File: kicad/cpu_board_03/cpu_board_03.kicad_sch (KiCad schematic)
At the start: 63 parts, among them J1 DIN41612_02x32_AC, J10 PLD_aux, J11 Conn_01x09, J6 Conn_01x02_Socket, J9 Ram1 Enable, SW1 SW_Reset, SW2 SW_PWR, U1 W65C02SxP, U10 74HC245, U11 74HC245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

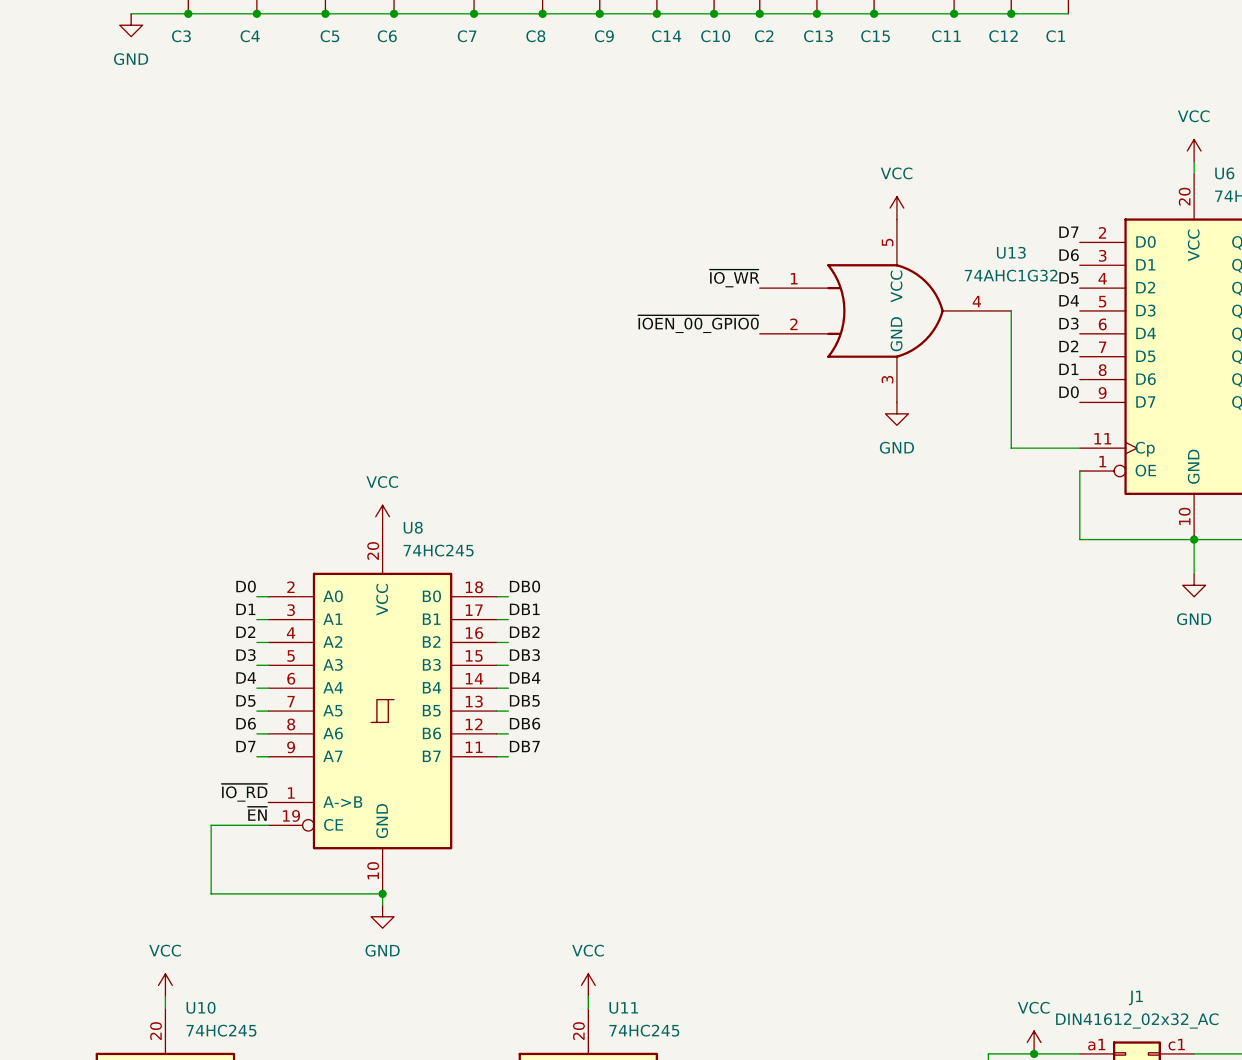
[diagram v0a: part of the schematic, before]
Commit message: add bus tranceiver OE signal
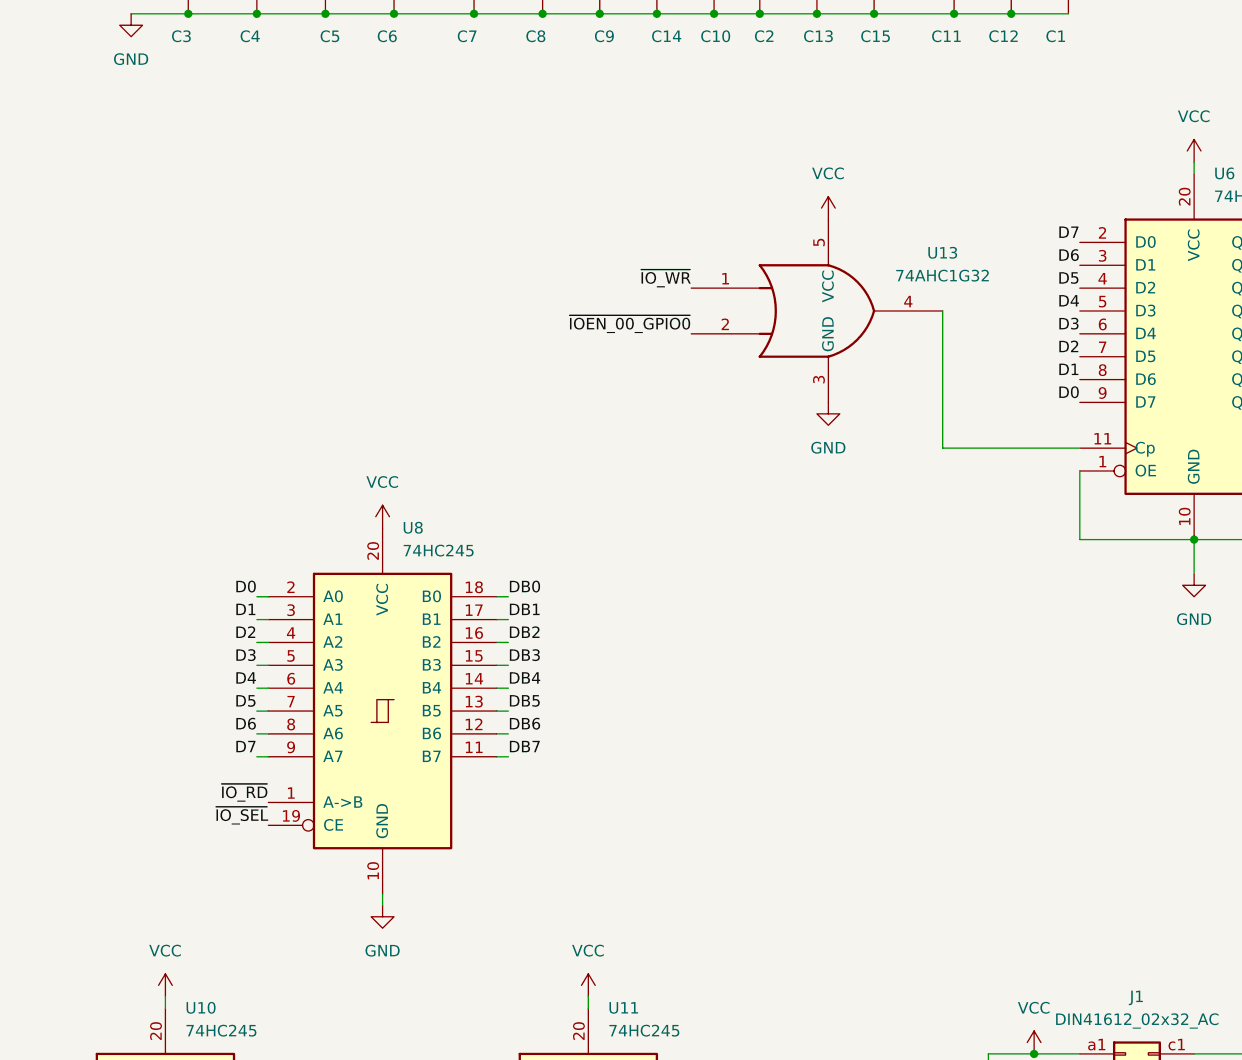
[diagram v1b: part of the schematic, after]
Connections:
- net GND: no longer U8.19 (CE)
- net ~{IO_SEL}: now also U8.19 (CE)
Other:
- moved on the sheet: U13
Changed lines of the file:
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@@
 	)
 	(junction
-		(at 271.78 147.32)
-		(diameter 0)
-		(color 0 0 0 0)
-	)
-	(junction
 		(at 261.62 241.3)
 		(diameter 0)
@@
 	(wire
 		(pts
-			(xy 252.73 147.32) (xy 252.73 139.7)
-		)
-		(stroke
-			(width 0)
-			(type default)
-		)
-	)
-	(wire
-		(pts
 			(xy 313.69 41.91) (xy 320.04 41.91)
 		)
@@
 	(wire
 		(pts
-			(xy 252.73 139.7) (xy 259.08 139.7)
-		)
-		(stroke
-			(width 0)
-			(type default)
-		)
-	)
-	(wire
-		(pts
 			(xy 271.78 228.6) (xy 278.13 228.6)
 		)
@@
 	(wire
 		(pts
-			(xy 341.63 82.55) (xy 341.63 97.79)
+			(xy 334.01 82.55) (xy 334.01 97.79)
 		)
 		(stroke
@@
 	(wire
 		(pts
-			(xy 271.78 147.32) (xy 252.73 147.32)
-		)
-		(stroke
-			(width 0)
-			(type default)
-		)
-	)
-	(wire
-		(pts
-			(xy 341.63 97.79) (xy 349.25 97.79)
+			(xy 334.01 97.79) (xy 349.25 97.79)
 		)
 		(stroke
@@
 		)
 	)
-	(label "~{EN}"
-		(at 259.08 139.7 180)
-		(effects
-			(font
-				(size 1.27 1.27)
-			)
-			(justify right bottom)
-		)
-	)
 	(label "D2"
 		(at 162.56 140.97 0)
@@
 	)
 	(label "~{IO_WR}"
-		(at 313.69 80.01 180)
+		(at 306.07 80.01 180)
 		(effects
 			(font
@@
 		)
 	)
+	(label "~{IO_SEL}"
+		(at 259.08 139.7 180)
+		(effects
+			(font
+				(size 1.27 1.27)
+			)
+			(justify right bottom)
+		)
+	)
 	(label "A11"
 		(at 134.62 163.83 180)
@@
 	)
 	(label "~{IOEN_00_GPIO0}"
-		(at 313.69 85.09 180)
+		(at 306.07 85.09 180)
 		(effects
 			(font
@@
 	(symbol
 		(lib_id "74xGxx:74AHC1G32")
-		(at 328.93 82.55 0)
+		(at 321.31 82.55 0)
 		(unit 1)
 		(exclude_from_sim no)
@@
 		(fields_autoplaced yes)
 		(property "Reference" "U13"
-			(at 341.63 76.1298 0)
+			(at 334.01 76.1298 0)
 			(effects
 				(font
@@
 		)
 		(property "Value" "74AHC1G32"
-			(at 341.63 78.6698 0)
+			(at 334.01 78.6698 0)
 			(effects
 				(font
@@
 		)
 		(property "Footprint" "Package_TO_SOT_SMD:SOT-23-5_HandSoldering"
-			(at 328.93 82.55 0)
+			(at 321.31 82.55 0)
 			(effects
 				(font
@@
 		)
 		(property "Datasheet" "http://www.ti.com/lit/sg/scyt129e/scyt129e.pdf"
-			(at 328.93 82.55 0)
+			(at 321.31 82.55 0)
 			(effects
 				(font
@@
 		)
 		(property "Description" "Single OR Gate, Low-Voltage CMOS"
-			(at 328.93 82.55 0)
+			(at 321.31 82.55 0)
 			(effects
 				(font
@@
 	(symbol
 		(lib_id "power:GND")
-		(at 328.93 92.71 0)
+		(at 321.31 92.71 0)
 		(unit 1)
 		(exclude_from_sim no)
@@
 		(fields_autoplaced yes)
 		(property "Reference" "#PWR042"
-			(at 328.93 99.06 0)
+			(at 321.31 99.06 0)
 			(effects
 				(font
@@
 		)
 		(property "Value" "GND"
-			(at 328.93 97.79 0)
+			(at 321.31 97.79 0)
 			(effects
 				(font
@@
 		)
 		(property "Footprint" ""
-			(at 328.93 92.71 0)
+			(at 321.31 92.71 0)
 			(effects
 				(font
@@
 		)
 		(property "Datasheet" ""
-			(at 328.93 92.71 0)
+			(at 321.31 92.71 0)
 			(effects
 				(font
@@
 		)
 		(property "Description" ""
-			(at 328.93 92.71 0)
+			(at 321.31 92.71 0)
 			(effects
 				(font
@@
 	(symbol
 		(lib_id "power:VCC")
-		(at 328.93 72.39 0)
+		(at 321.31 72.39 0)
 		(unit 1)
 		(exclude_from_sim no)
@@
 		(fields_autoplaced yes)
 		(property "Reference" "#PWR045"
-			(at 328.93 76.2 0)
+			(at 321.31 76.2 0)
 			(effects
 				(font
@@
 		)
 		(property "Value" "VCC"
-			(at 328.93 67.31 0)
+			(at 321.31 67.31 0)
 			(effects
 				(font
@@
 		)
 		(property "Footprint" ""
-			(at 328.93 72.39 0)
+			(at 321.31 72.39 0)
 			(effects
 				(font
@@
 		)
 		(property "Datasheet" ""
-			(at 328.93 72.39 0)
+			(at 321.31 72.39 0)
 			(effects
 				(font
@@
 		)
 		(property "Description" ""
-			(at 328.93 72.39 0)
+			(at 321.31 72.39 0)
 			(effects
 				(font

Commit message: route latest changes
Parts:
- removed J10: PLD_aux, Connector_PinHeader_2.54mm:PinHeader_1x03_P2.54mm_Vertical, symbol Connector:Conn_01x03_Socket
- removed R8: 10K, Resistor_SMD:R_0805_2012Metric_Pad1.20x1.40mm_HandSolder, symbol Device:R
- removed U11: 74HC245, Package_SO:SO-20_12.8x7.5mm_P1.27mm, symbol 74xx:74HC245
- removed U12: 74LS138, Package_SO:SO-16_3.9x9.9mm_P1.27mm, symbol 74xx:74LS138
- added JP1, JP2: SolderJumper_3_Open, Jumper:SolderJumper-3_P1.3mm_Bridged12_RoundedPad1.0x1.5mm_NumberLabels, symbol Jumper:SolderJumper_3_Bridged12
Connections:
- net AB10 is gone; now on net AB2: J1.a13 (Pin_a13)
- net AB11 is gone; now on net AB3: J1.c13 (Pin_c13)
- net AB12 is gone; now on net AB4: J1.a12 (Pin_a12)
- net AB13 is gone; now on net ~{IO_RD}: J1.c12 (Pin_c12)
- net AB14 is gone; now on net ~{IO_WR}: J1.a11 (Pin_a11)
- net AB8 is gone; now on net AB0: J1.a14 (Pin_a14)
- net AB9 is gone; now on net AB1: J1.c14 (Pin_c14)
- net ~{IOEN_12} is gone; now on net RDY: J1.a22 (Pin_a22)
- net ~{IOEN_13} is gone; now on net ~{IRQ}: J1.c22 (Pin_c22)
- net ~{IOEN_14} is gone; now on net ~{NMI}: J1.a21 (Pin_a21)
- net ~{IOEN_15} is gone; now on net SYNC: J1.c21 (Pin_c21)
- net A4: no longer U5.1 (A0)
- net A5: now also U5.1 (A0); no longer U10.13 (B5), U5.2 (A1)
- net A6: now also U5.2 (A1); no longer U10.12 (B6), U5.3 (A2)
- net A7: now also U5.3 (A2); no longer U10.11 (B7), U5.5 (E2)
- net AB0: no longer J1.a18 (Pin_a18)
- net AB1: no longer J1.c18 (Pin_c18)
- net AB2: no longer J1.a17 (Pin_a17)
- net AB3: no longer J1.c17 (Pin_c17)
- net AB4: no longer J1.a16 (Pin_a16)
- net CLOCK: now also J1.a7 (Pin_a7)
- net GND: now also J1.c15 (Pin_c15), U5.5 (E2); no longer J1.c19 (Pin_c19)
- net PLD_I1: now also J1.c9 (Pin_c9)
- net RDY: no longer J1.c29 (Pin_c29)
- net SYS_CLK: now also U4.23 (O0); no longer J1.a7 (Pin_a7), U4.15 (O8)
- net VCC: now also J1.a15 (Pin_a15); no longer J1.a19 (Pin_a19)
- net ~{IOEN_00_GPIO0}: now also J1.a19 (Pin_a19), U13.1; no longer J1.a28 (Pin_a28), U13.2
- net ~{IOEN_01}: now also J1.c19 (Pin_c19); no longer J1.c28 (Pin_c28)
- net ~{IOEN_02_UART}: now also J1.a18 (Pin_a18); no longer J1.a27 (Pin_a27)
- net ~{IOEN_03}: now also J1.c18 (Pin_c18); no longer J1.c27 (Pin_c27)
- net ~{IOEN_04}: now also J1.a17 (Pin_a17); no longer J1.a26 (Pin_a26)
- net ~{IOEN_05}: now also J1.c17 (Pin_c17); no longer J1.c26 (Pin_c26)
- net ~{IOEN_06}: now also J1.a16 (Pin_a16); no longer J1.a25 (Pin_a25)
- net ~{IOEN_07}: now also J1.c16 (Pin_c16); no longer J1.c25 (Pin_c25)
- net ~{IO_RD}: now also U10.7 (A5); no longer J1.c8 (Pin_c8), U4.16 (O7)
- net ~{IO_SEL}: now also U10.11 (B7); no longer J1.a8 (Pin_a8)
- net ~{IO_WR}: now also U10.8 (A6), U13.2; no longer J1.c7 (Pin_c7), U13.1, U4.14 (O9)
- net ~{IRQ}: no longer J1.a29 (Pin_a29)
- net ~{NMI}: no longer J1.c30 (Pin_c30)
- net ~{OE}: now also JP1.1 (A)
- net ~{QWE}: now also JP2.1 (A)
- net SYNC: now reaches U1.7 (SYNC)
- net AB15 renamed ~{IO_SEL_BUS}
- net ~{IO_SEL_BUS}: now also U10.9 (A7)
- removed net AB5: J1.c16 (Pin_c16), U10.7 (A5)
- removed net AB6: J1.a15 (Pin_a15), U10.8 (A6)
- removed net AB7: J1.c15 (Pin_c15), U10.9 (A7)
- net BE: no longer names the net of U1.36 (BE)
- net BE: no longer J1.a30 (Pin_a30)
- removed net PLD_O0: J1.c9 (Pin_c9), U4.23 (O0)
- net ~{IOEN_08}: no longer names the net of J1.a24 (Pin_a24)
- net ~{IOEN_09}: no longer names the net of J1.c24 (Pin_c24)
- net ~{IOEN_10}: no longer names the net of J1.a23 (Pin_a23)
- net ~{IOEN_11}: no longer names the net of J1.c23 (Pin_c23)
- new net: JP2.2 (C), U10.12 (B6)
- new net: JP1.2 (C), U10.13 (B5)
- new net PLD_O7: J1.c8 (Pin_c8), JP1.3 (B), U4.16 (O7)
- new net PLD_O8: J1.a8 (Pin_a8), JP2.3 (B), U4.15 (O8)
- new net PLD_O9: J1.c7 (Pin_c7), U4.14 (O9)
- no-connect marks 12 -> 14

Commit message: finished basic routing
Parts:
- added J2: Clock, Connector_PinSocket_2.54mm:PinSocket_1x02_P2.54mm_Vertical, symbol Connector:Conn_01x02_Socket
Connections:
- net CLOCK: now also J2.2 (Pin_2); no longer J1.a7 (Pin_a7)
- net GND: now also J2.1 (Pin_1)
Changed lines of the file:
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@@
 	(generator_version "9.0")
 	(paper "A3")
-	(text_box "v2.1 update: connect ~{E2} to A7 to select onboard IO (IO0) only for io addresses 0x00 - 0x7f\n0x80-0xff can be used on external io board"
+	(text_box "v3 update: select IO port from highest 3 bits only."
 		(exclude_from_sim no)
 		(at 83.82 265.43 0)
@@
 		(stroke
 			(width 0)
-			(type default)
+			(type solid)
 		)
 		(fill
@@
 		)
 	)
+	(label "CLOCK"
+		(at 59.69 82.55 180)
+		(effects
+			(font
+				(size 1.27 1.27)
+			)
+			(justify right bottom)
+		)
+	)
 	(label "DB7"
 		(at 361.95 167.64 0)
@@
 		)
 	)
-	(label "CLOCK"
-		(at 349.25 180.34 180)
-		(effects
-			(font
-				(size 1.27 1.27)
-			)
-			(justify right bottom)
-		)
-	)
 	(label "A3"
 		(at 134.62 143.51 180)
@@
 	)
 	(symbol
+		(lib_id "power:GND")
+		(at 59.69 85.09 0)
+		(unit 1)
+		(exclude_from_sim no)
+		(in_bom yes)
+		(on_board yes)
+		(dnp no)
+		(fields_autoplaced yes)
+		(property "Reference" "#PWR027"
+			(at 59.69 91.44 0)
+			(effects
+				(font
+					(size 1.27 1.27)
+				)
+				(hide yes)
+			)
+		)
+		(property "Value" "GND"
+			(at 59.69 90.17 0)
+			(effects
+				(font
+					(size 1.27 1.27)
+				)
+			)
+		)
+		(property "Footprint" ""
+			(at 59.69 85.09 0)
+			(effects
+				(font
+					(size 1.27 1.27)
+				)
+				(hide yes)
+			)
+		)
+		(property "Datasheet" ""
+			(at 59.69 85.09 0)
+			(effects
+				(font
+					(size 1.27 1.27)
+				)
+				(hide yes)
+			)
+		)
+		(property "Description" ""
+			(at 59.69 85.09 0)
+			(effects
+				(font
+					(size 1.27 1.27)
+				)
+			)
+		)
+		(pin "1"
+		)
+		(instances
+			(project "cpu_board_03"
+				(path "/a9a73dc6-7f92-4458-9da8-49621d12e480"
+					(reference "#PWR027")
+					(unit 1)
+				)
+			)
+		)
+	)
+	(symbol
 		(lib_id "Device:C")
 		(at 265.43 45.72 0)
@@
 					(unit 1)
 				)
+			)
+		)
+	)
+	(symbol
+		(lib_id "Connector:Conn_01x02_Socket")
+		(at 64.77 85.09 0)
+		(mirror x)
+		(unit 1)
+		(exclude_from_sim no)
+		(in_bom yes)
+		(on_board yes)
+		(dnp no)
+		(property "Reference" "J2"
+			(at 67.818 86.868 0)
+			(effects
+				(font
+					(size 1.27 1.27)
+				)
+			)
+		)
+		(property "Value" "Clock"
+			(at 62.23 85.09 90)
+			(effects
+				(font
+					(size 1.27 1.27)
+				)
+			)
+		)
+		(property "Footprint" "Connector_PinSocket_2.54mm:PinSocket_1x02_P2.54mm_Vertical"
+			(at 64.77 85.09 0)
+			(effects
+				(font
+					(size 1.27 1.27)
+				)
+				(hide yes)
+			)
+		)
+		(property "Datasheet" "~"
+			(at 64.77 85.09 0)
+			(effects
+				(font
+					(size 1.27 1.27)
+				)
+				(hide yes)
+			)
+		)
+		(property "Description" "Generic connector, single row, 01x02, script generated"
+			(at 64.77 85.09 0)
+			(effects
+				(font
+					(size 1.27 1.27)
+				)
+				(hide yes)
+			)
+		)
+		(pin "1"
+		)
+		(pin "2"
+		)
+		(instances
+			(project "cpu_board_03"
+				(path "/a9a73dc6-7f92-4458-9da8-49621d12e480"
+					(reference "J2")
+					(unit 1)
+				)

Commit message: finished drc errors
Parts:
- removed C15: 100nF, Capacitor_SMD:C_0805_2012Metric_Pad1.18x1.45mm_HandSolder, symbol Device:C
- added JP3: SolderJumper_3_Open, Jumper:SolderJumper-3_P1.3mm_Open_RoundedPad1.0x1.5mm, symbol Jumper:SolderJumper_3_Open
- JP1, JP2: footprint Jumper:SolderJumper-3_P1.3mm_Bridged12_RoundedPad1.0x1.5mm_NumberLabels -> Jumper:SolderJumper-3_P1.3mm_Open_RoundedPad1.0x1.5mm; symbol Jumper:SolderJumper_3_Bridged12 -> Jumper:SolderJumper_3_Open
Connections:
- net A4: now also JP3.3 (B)
- net GND: now also JP3.1 (A); no longer U5.5 (E2)
- new net: JP3.2 (C), U5.5 (E2)
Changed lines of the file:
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@@
 	(text_box "v3 update: select IO port from highest 3 bits only."
 		(exclude_from_sim no)
-		(at 83.82 265.43 0)
+		(at 68.58 276.86 0)
 		(size 24.13 17.78)
 		(margins 0.9525 0.9525 0.9525 0.9525)
@@
 	)
 	(junction
-		(at 326.39 49.53)
-		(diameter 0)
-		(color 0 0 0 0)
-	)
-	(junction
 		(at 361.95 107.95)
 		(diameter 0)
@@
 	)
 	(junction
-		(at 326.39 41.91)
-		(diameter 0)
-		(color 0 0 0 0)
-	)
-	(junction
 		(at 339.09 200.66)
 		(diameter 0)
@@
 	(wire
 		(pts
-			(xy 99.06 260.35) (xy 99.06 275.59)
+			(xy 95.25 254) (xy 95.25 255.27)
 		)
 		(stroke
@@
 	(wire
 		(pts
-			(xy 320.04 41.91) (xy 326.39 41.91)
+			(xy 339.09 187.96) (xy 339.09 200.66)
 		)
 		(stroke
@@
 	(wire
 		(pts
-			(xy 339.09 187.96) (xy 339.09 200.66)
+			(xy 128.27 25.4) (xy 135.89 25.4)
 		)
 		(stroke
@@
 	(wire
 		(pts
-			(xy 128.27 25.4) (xy 135.89 25.4)
+			(xy 92.71 254) (xy 95.25 254)
 		)
 		(stroke
@@
 	(wire
 		(pts
+			(xy 95.25 275.59) (xy 119.38 275.59)
+		)
+		(stroke
+			(width 0)
+			(type default)
+		)
+	)
+	(wire
+		(pts
 			(xy 25.4 266.7) (xy 35.56 266.7)
 		)
@@
 	(wire
 		(pts
-			(xy 99.06 275.59) (xy 119.38 275.59)
-		)
-		(stroke
-			(width 0)
-			(type default)
-		)
-	)
-	(wire
-		(pts
 			(xy 110.49 151.13) (xy 109.22 151.13)
 		)
@@
 	(wire
 		(pts
-			(xy 326.39 49.53) (xy 335.28 49.53)
+			(xy 320.04 49.53) (xy 335.28 49.53)
 		)
 		(stroke
@@
 	(wire
 		(pts
-			(xy 326.39 41.91) (xy 335.28 41.91)
+			(xy 320.04 41.91) (xy 335.28 41.91)
 		)
 		(stroke
@@
 	(wire
 		(pts
-			(xy 320.04 49.53) (xy 326.39 49.53)
-		)
-		(stroke
-			(width 0)
-			(type default)
-		)
-	)
-	(wire
-		(pts
 			(xy 273.05 242.57) (xy 278.13 242.57)
 		)
@@
 	(wire
 		(pts
+			(xy 95.25 275.59) (xy 95.25 265.43)
+		)
+		(stroke
+			(width 0)
+			(type default)
+		)
+	)
+	(wire
+		(pts
 			(xy 58.42 121.92) (xy 57.15 121.92)
 		)
@@
 		)
 	)
+	(label "A4"
+		(at 92.71 254 0)
+		(effects
+			(font
+				(size 1.27 1.27)
+			)
+			(justify left bottom)
+		)
+	)
 	(label "DB6"
 		(at 349.25 167.64 180)
@@
 	)
 	(symbol
-		(lib_id "Device:C")
-		(at 326.39 45.72 0)
-		(unit 1)
-		(exclude_from_sim no)
-		(in_bom yes)
-		(on_board yes)
-		(dnp no)
-		(property "Reference" "C15"
-			(at 328.295 52.07 0)
-			(effects
-				(font
-					(size 1.27 1.27)
-				)
-				(justify right)
-			)
-		)
-		(property "Value" "100nF"
-			(at 328.93 39.37 0)
-			(effects
-				(font
-					(size 1.27 1.27)
-				)
-				(justify right)
-			)
-		)
-		(property "Footprint" "Capacitor_SMD:C_0805_2012Metric_Pad1.18x1.45mm_HandSolder"
-			(at 327.3552 49.53 0)
-			(effects
-				(font
-					(size 1.27 1.27)
-				)
-				(hide yes)
-			)
-		)
-		(property "Datasheet" "~"
-			(at 326.39 45.72 0)
-			(effects
-				(font
-					(size 1.27 1.27)
-				)
-				(hide yes)
-			)
-		)
-		(property "Description" ""
-			(at 326.39 45.72 0)
-			(effects
-				(font
-					(size 1.27 1.27)
-				)
-			)
-		)
-		(pin "1"
-		)
-		(pin "2"
-		)
-		(instances
-			(project "cpu_board_03"
-				(path "/a9a73dc6-7f92-4458-9da8-49621d12e480"
-					(reference "C15")
-					(unit 1)
-				)
-			)
-		)
-	)
-	(symbol
 		(lib_id "74xx:74LS138")
 		(at 119.38 252.73 0)
@@
 	)
 	(symbol
+		(lib_id "Jumper:SolderJumper_3_Open")
+		(at 95.25 260.35 90)
+		(unit 1)
+		(exclude_from_sim no)
+		(in_bom yes)
+		(on_board yes)
+		(dnp no)
+		(fields_autoplaced yes)
+		(property "Reference" "JP3"
+			(at 92.71 259.0799 90)
+			(effects
+				(font
+					(size 1.27 1.27)
+				)
+				(justify left)
+			)
+		)
+		(property "Value" "SolderJumper_3_Open"
+			(at 92.71 261.6199 90)
+			(effects
+				(font
+					(size 1.27 1.27)
+				)
+				(justify left)
+			)
+		)
+		(property "Footprint" "Jumper:SolderJumper-3_P1.3mm_Open_RoundedPad1.0x1.5mm"
+			(at 95.25 260.35 0)
+			(effects
+				(font
+					(size 1.27 1.27)
+				)
+				(hide yes)
+			)
+		)
+		(property "Datasheet" "~"
+			(at 95.25 260.35 0)
+			(effects
+				(font
+					(size 1.27 1.27)
+				)
+				(hide yes)
+			)
+		)
+		(property "Description" "Solder Jumper, 3-pole, open"
+			(at 95.25 260.35 0)
+			(effects
+				(font
+					(size 1.27 1.27)
+				)
+				(hide yes)
+			)
+		)
+		(pin "3"
+		)
+		(pin "2"
+		)
+		(pin "1"
+		)
+		(instances
+			(project "cpu_board_03"
+				(path "/a9a73dc6-7f92-4458-9da8-49621d12e480"
+					(reference "JP3")
+					(unit 1)
+				)
+			)
+		)
+	)
+	(symbol
 		(lib_id "Device:C")
 		(at 257.81 45.72 0)
@@
 	)
 	(symbol
-		(lib_id "Jumper:SolderJumper_3_Bridged12")
+		(lib_id "Jumper:SolderJumper_3_Open")
 		(at 279.4 195.58 270)
 		(unit 1)
@@
 			)
 		)
-		(property "Footprint" "Jumper:SolderJumper-3_P1.3mm_Bridged12_RoundedPad1.0x1.5mm_NumberLabels"
+		(property "Footprint" "Jumper:SolderJumper-3_P1.3mm_Open_RoundedPad1.0x1.5mm"
 			(at 279.4 195.58 0)
 			(effects
@@
 			)
 		)
-		(property "Description" "3-pole Solder Jumper, pins 1+2 closed/bridged"
+		(property "Description" "Solder Jumper, 3-pole, open"
 			(at 279.4 195.58 0)
 			(effects
@@
 	)
 	(symbol
-		(lib_id "Jumper:SolderJumper_3_Bridged12")
+		(lib_id "Jumper:SolderJumper_3_Open")
 		(at 279.4 180.34 270)
 		(unit 1)
@@
 			)
 		)
-		(property "Footprint" "Jumper:SolderJumper-3_P1.3mm_Bridged12_RoundedPad1.0x1.5mm_NumberLabels"
+		(property "Footprint" "Jumper:SolderJumper-3_P1.3mm_Open_RoundedPad1.0x1.5mm"
 			(at 279.4 180.34 0)
 			(effects
@@
 			)
 		)
-		(property "Description" "3-pole Solder Jumper, pins 1+2 closed/bridged"
+		(property "Description" "Solder Jumper, 3-pole, open"
 			(at 279.4 180.34 0)
 			(effects
